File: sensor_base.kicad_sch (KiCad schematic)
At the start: 41 parts, among them J2 Conn_Coaxial, U1 MCP3204, U10 REF3040, U11 INA333xxDGK, U15 M24C02-WMN, U2 INA333xxDGK, U3 TPS22929D, U4 INA333xxDGK, U5 INA333xxDGK, U9 REF3025

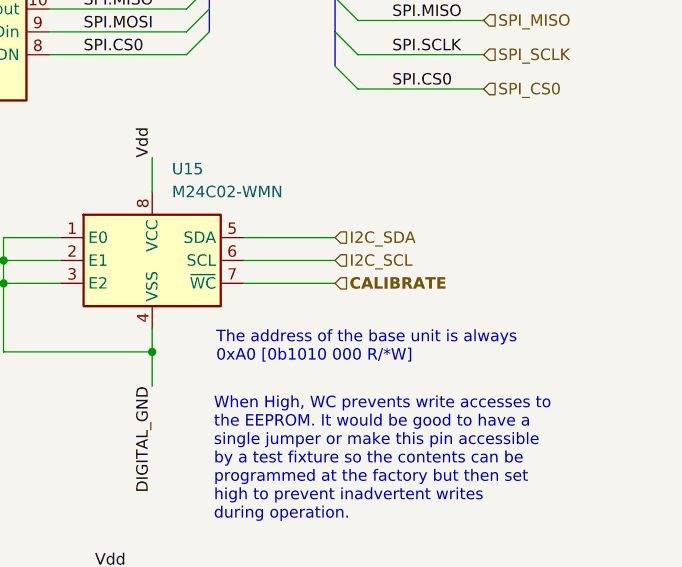
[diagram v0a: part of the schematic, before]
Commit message: Sensor board basic updates
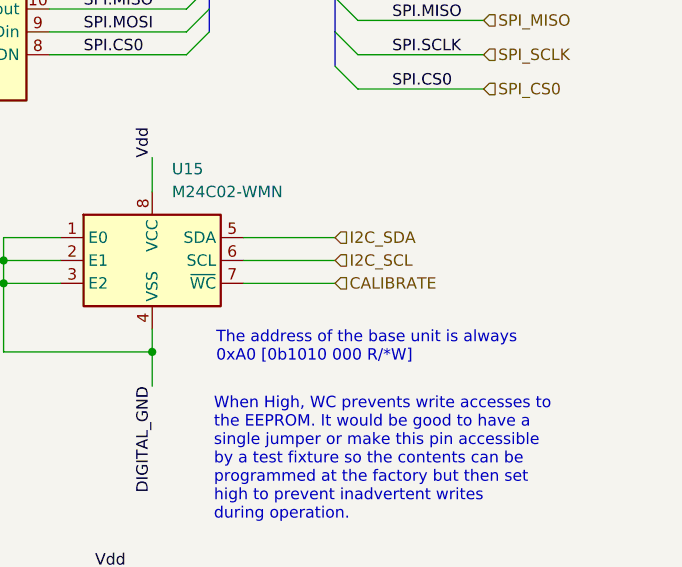
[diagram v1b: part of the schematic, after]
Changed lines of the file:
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@@
 			(font
 				(size 1.27 1.27)
-				(thickness 0.254)
-				(bold yes)
+				(thickness 0.1588)
 			)
 			(justify left)

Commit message: Split the sensor modules into a 4 and 8 port version. Fleshed out the power module a bit more. Started adding sensor board connectors to the root schematic and started pulling out sensor boards to their own, separate module. Began wiring up the root schematic to get my bearings a bit.
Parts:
- added C27, C28: C, symbol Device:C
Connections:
- net ANALOG_GND: now also C10.2, C11.2, C12.2, C13.2, C19.2, C21.2, C22.2, C5.2, C6.2, C7.2, C8.2, C9.2, C27.2, C28.2
- net DIGITAL_GND: now also C14.2, C15.2, C16.2, C17.2, C18.2, C20.2
- net Vdd: now also C10.1, C11.1, C12.1, C13.1, C14.1, C15.1, C16.1, C17.1, C18.1, C19.1, C20.1, C9.1
- net Vref_2.5: now also C21.1, C22.1, C5.1, C6.1
- net Vref_4.096: now also C7.1, C8.1, C27.1, C28.1
- net ENABLE/*SHDN renamed ENABLE/~{SHDN}
- net SPI_CS0 renamed SPI_CS
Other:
- note added: "Decoupling Capacitors are connected as close as possible to each IC of the given power domain."
- note added: "TBD"
- moved on the sheet: C14, C15, C16, C17, C18, C20, C21, C22, C5, C6, C7, C8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

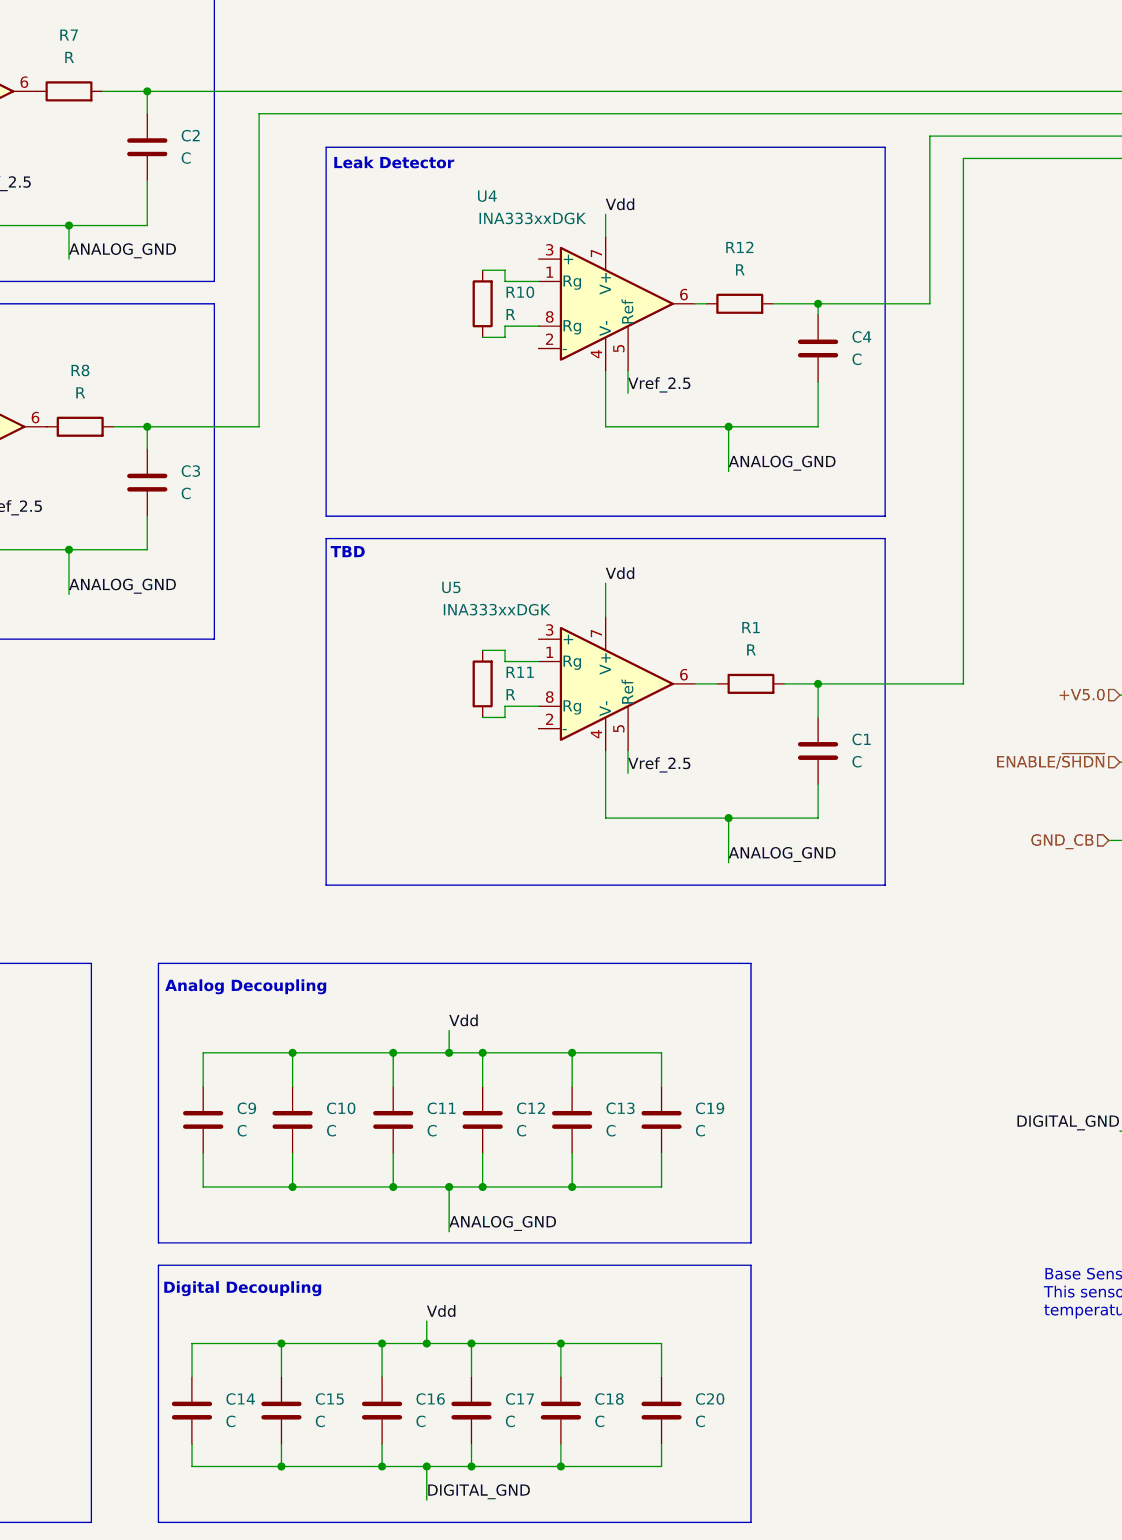
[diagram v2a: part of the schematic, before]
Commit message: Cleaned up some signal lines in the sensor board. Shuffled the decoupling caps around a bit as well as rearranged the EEPROM and power supply for clarity. Added buffered 2.5V offset to the pH and ORP circuits. Swapped one TBD input on the base sensor and sensor_4 boards for an ADC calibration input.
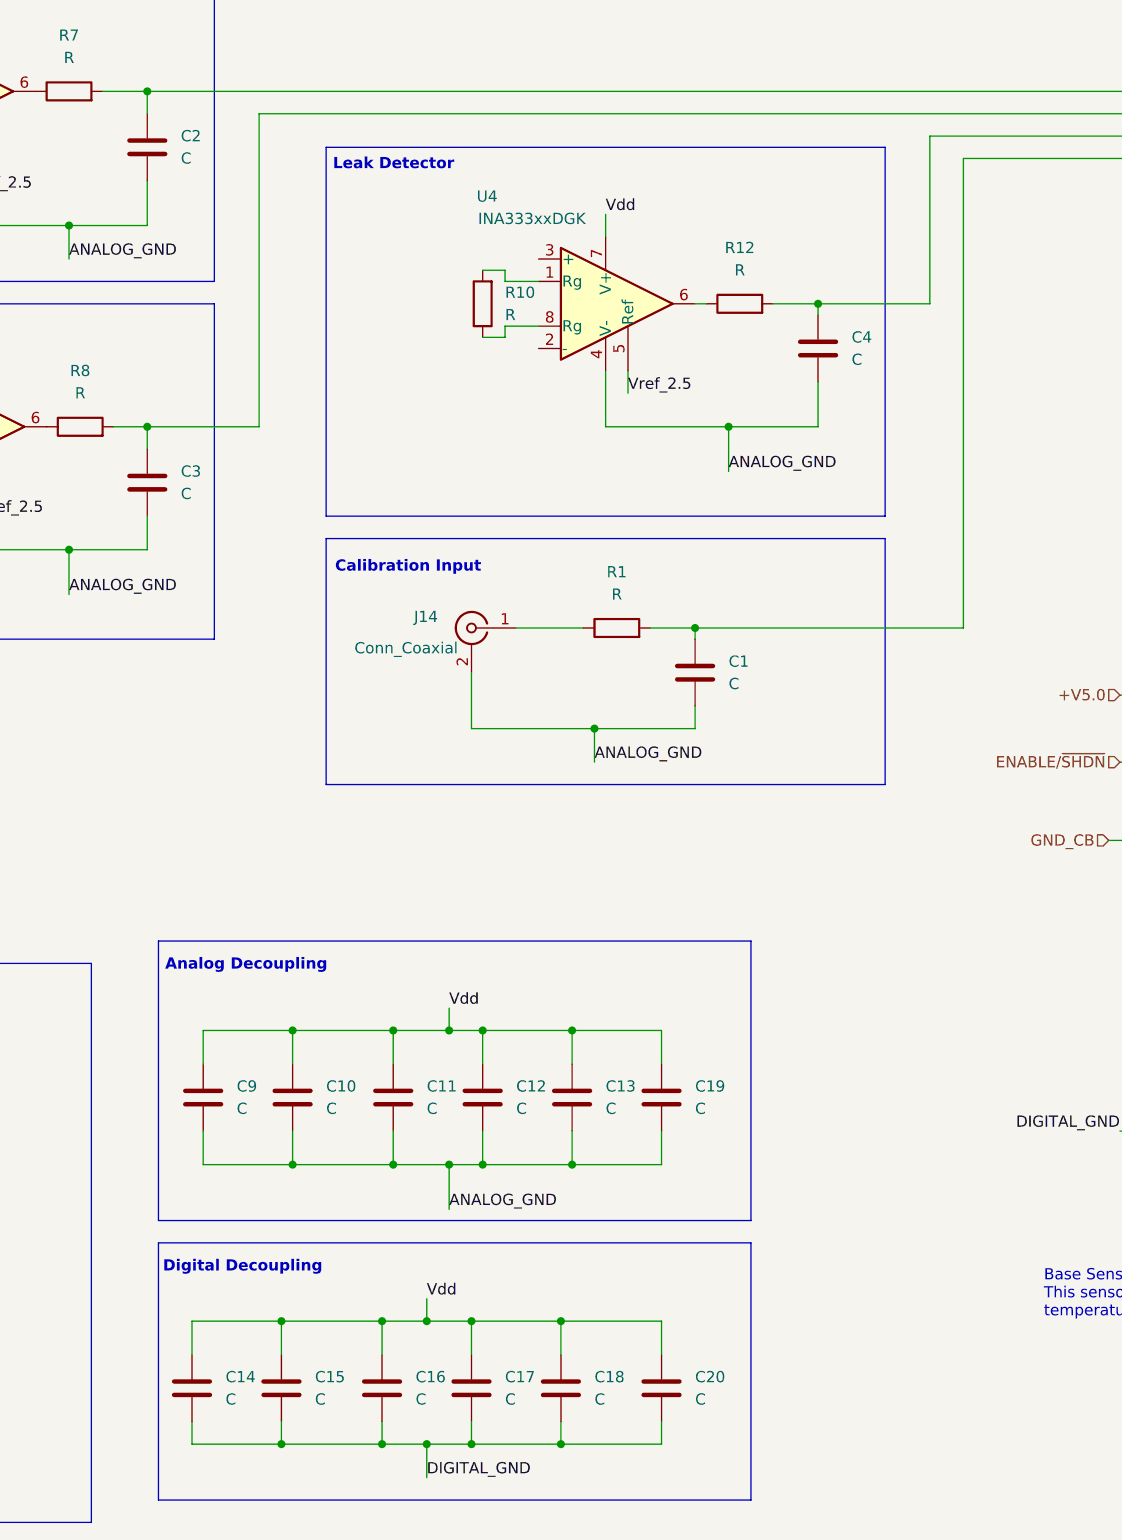
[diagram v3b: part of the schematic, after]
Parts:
- removed R11: R, symbol Device:R
- removed U5: INA333xxDGK, Package_SO:VSSOP-8_3x3mm_P0.65mm, symbol Amplifier_Instrumentation:INA333xxDGK
- added J14: Conn_Coaxial, symbol Connector:Conn_Coaxial
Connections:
- net ANALOG_GND: now also J14.2 (Ext)
- net at R1.1: now also J14.1 (In)
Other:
- note added: "Calibration Input"
- note removed: "TBD"
- moved on the sheet: C10, C11, C12, C13, C14, C15, C16, C17, C18, C19, C20, C9

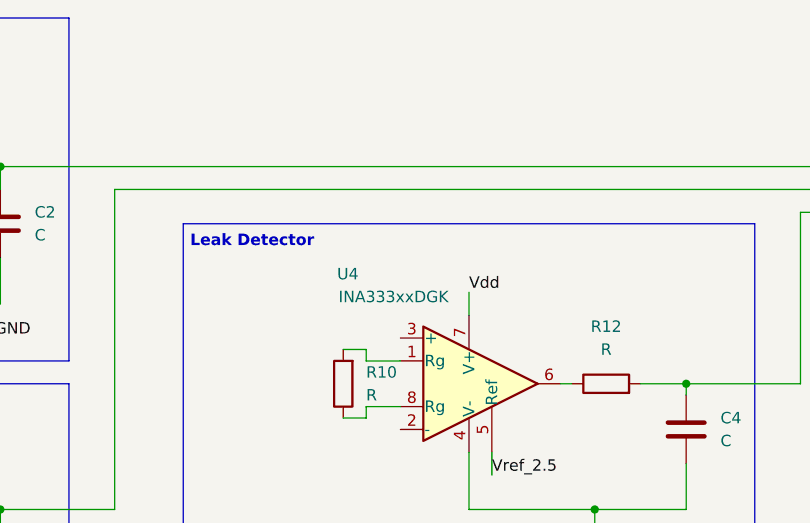
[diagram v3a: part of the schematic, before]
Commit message: Added some notes to otherwise blank pages. Added the full 8 sensor buffers to the 8 sensor analog board. Added a decoupling sub page to same. Changed a couple of sensor labels on base and 4 board just as placeholders
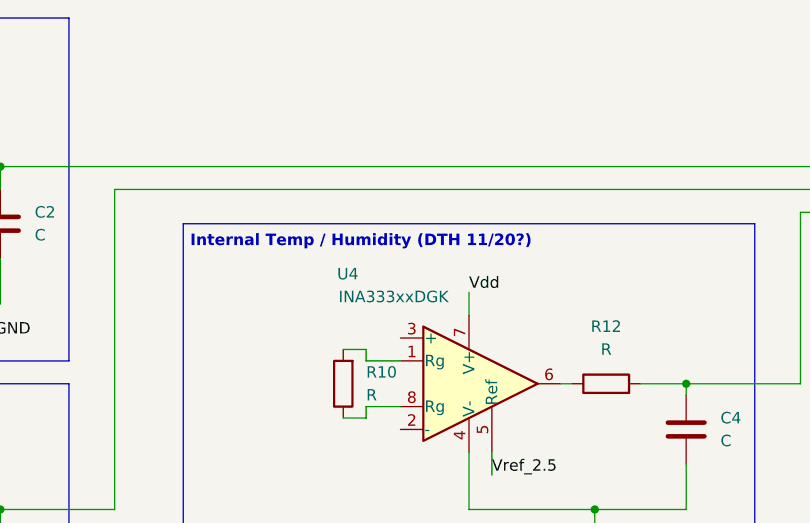
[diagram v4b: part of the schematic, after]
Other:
- note added: "Internal Temp / Humidity (DTH 11/20?)"
- note removed: "Leak Detector"
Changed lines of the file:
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@@
 		)
 	)
-	(text "Leak Detector"
+	(text "Internal Temp / Humidity (DTH 11/20?)"
 		(exclude_from_sim no)
 		(at 97.282 42.672 0)

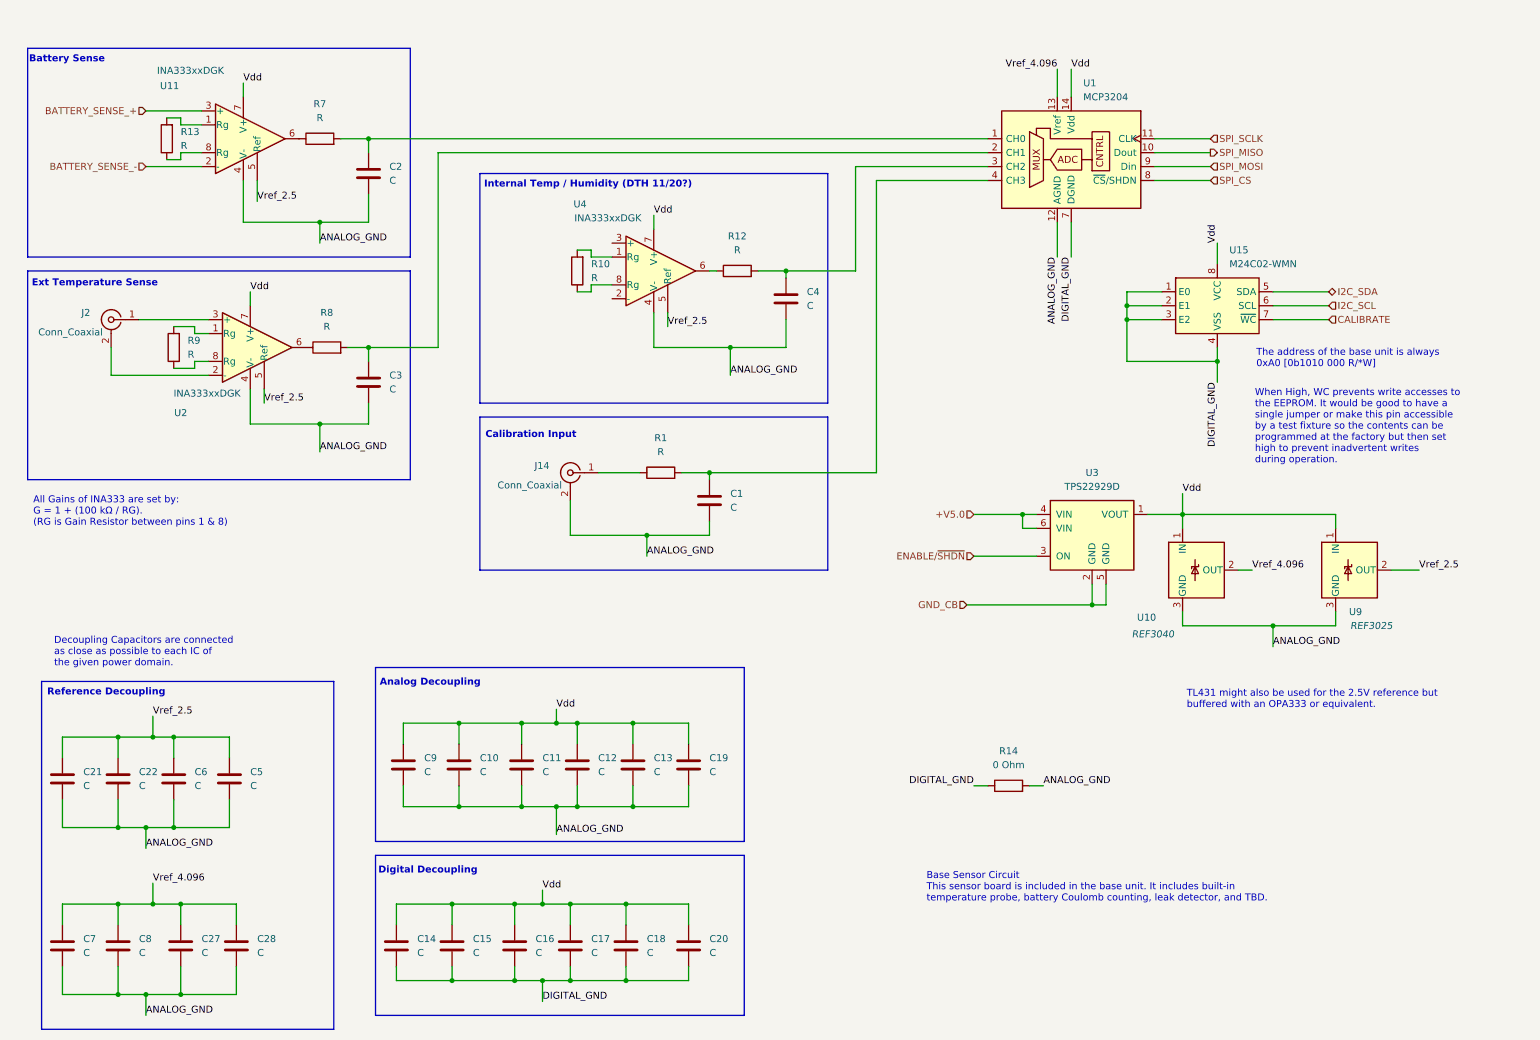
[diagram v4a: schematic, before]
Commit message: Updated the ORP and pH probes with a more appropriate amp. Added some notes. Added a tentative PL-100 adapter circuit. Added Vref buffering. Started move towards ESP32 ADC converter for base sensors.
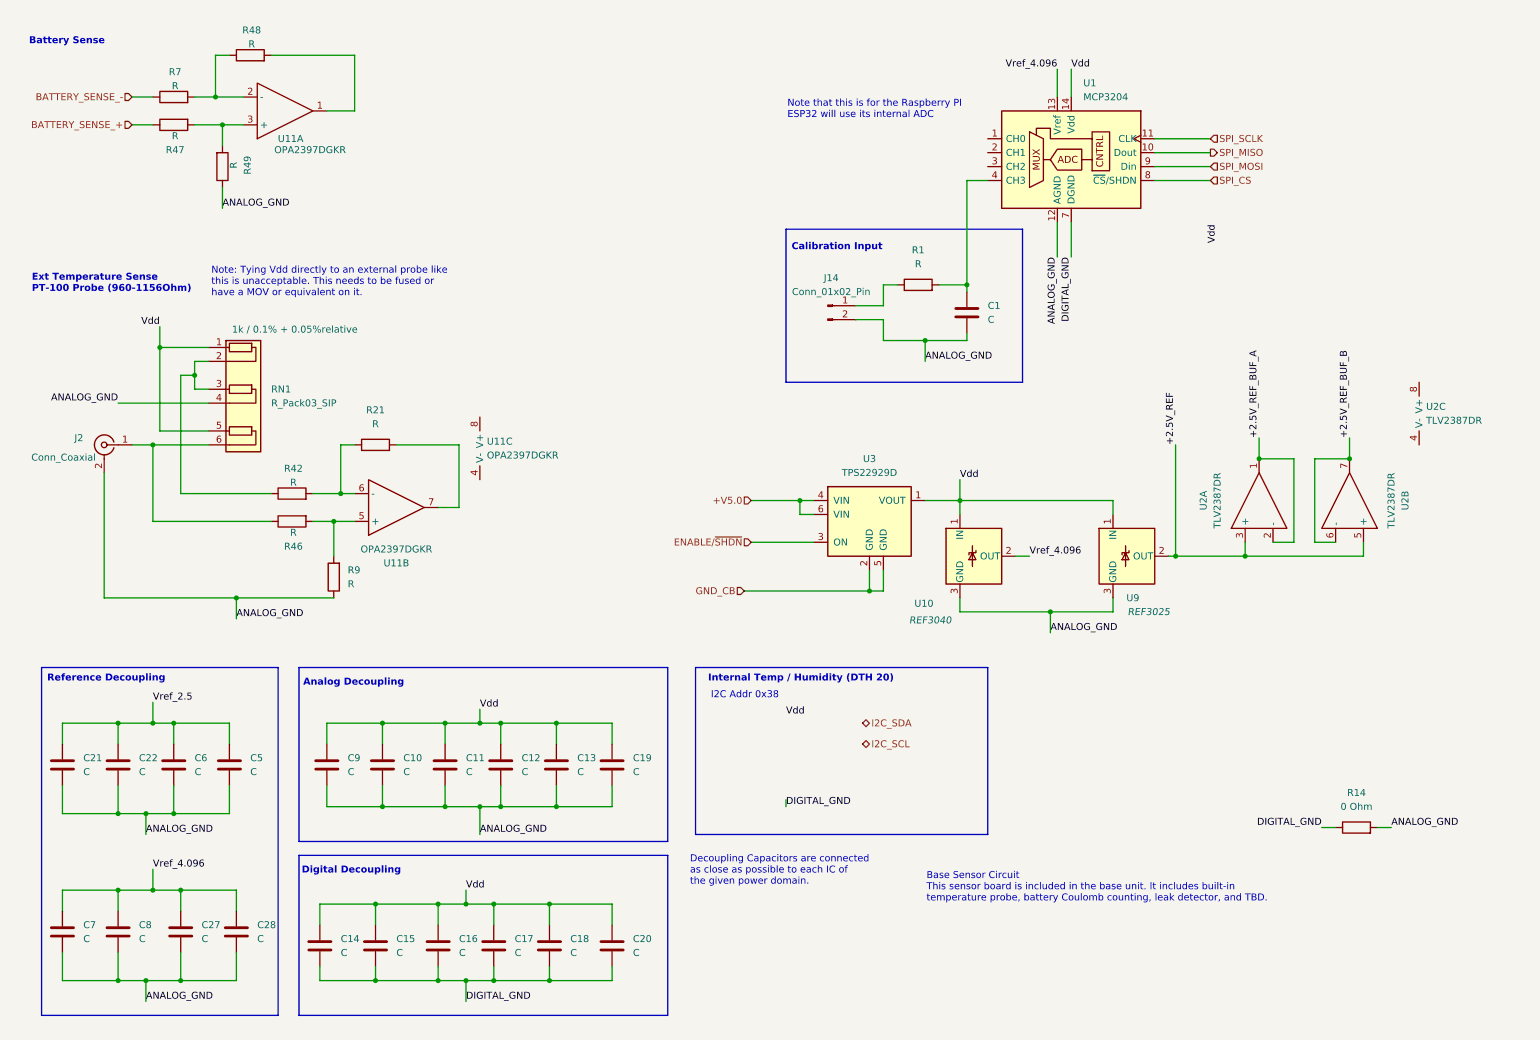
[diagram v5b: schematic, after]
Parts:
- removed C2, C3, C4: C, symbol Device:C
- removed J14: Conn_Coaxial, symbol Connector:Conn_Coaxial
- removed R10, R12, R13, R8: R, symbol Device:R
- removed U11, U2, U4: INA333xxDGK, Package_SO:VSSOP-8_3x3mm_P0.65mm, symbol Amplifier_Instrumentation:INA333xxDGK
- removed U15: M24C02-WMN, Package_SO:SOIC-8_3.9x4.9mm_P1.27mm, symbol Memory_EEPROM:M24C02-WMN
- added J14: Conn_01x02_Pin, symbol Connector:Conn_01x02_Pin
- added R21, R42, R46, R47, R48, R49: R, symbol Device:R
- added RN1: R_Pack03_SIP, Resistor_THT:R_Array_SIP6, symbol Device:R_Pack03_SIP
- added U11: OPA2397DGKR, Package_SO:SOIC-8_3.9x4.9mm_P1.27mm, symbol Op-Amp-Extended:OPA2397DR
- added U2: TLV2387DR, Package_SO:SOIC-8_3.9x4.9mm_P1.27mm, symbol Op-Amp-Extended:TLV2387DR
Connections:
- net ANALOG_GND: now also J2.2 (Ext), R9.1, J14.2 (Pin_2), R49.1, RN1.4 (R2.2)
- net BATTERY_SENSE_+: now also R47.1
- net BATTERY_SENSE_-: now also R7.1
- net Vdd: now also RN1.1 (R1.1), RN1.5 (R3.1)
- net Vref_2.5: no longer U9.2 (OUT)
- net at R7.2: now also R48.1, U11.2 (-); no longer U1.1 (CH0)
- net at J2.1 (In): now also R46.1, RN1.6 (R3.2)
- net at R1.1: now also J14.1 (Pin_1)
- net at R9.2: now also R46.2, U11.5 (+)
- new net: R48.2, U11.1
- new net: R21.1, R42.2, U11.6 (-)
- new net: R21.2, U11.7
- new net: R47.2, R49.2, U11.3 (+)
- new net: R42.1, RN1.2 (R1.2), RN1.3 (R2.1)
- new net +2.5V_REF: U2.3 (+), U2.5 (+), U9.2 (OUT)
- new net +2.5V_REF_BUF_A: U2.1, U2.2 (-)
- new net +2.5V_REF_BUF_B: U2.6 (-), U2.7
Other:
- note added: "Ext Temperature Sense PT-100 Probe (960-1156Ohm)"
- note added: "I2C Addr 0x38"
- note added: "Internal Temp / Humidity (DTH 20)"
- note added: "Note that this is for the Raspberry PI ESP32 will use its internal ADC"
- note added: "Note: Tying Vdd directly to an external probe like this is unacceptable. This needs to be fused or have a MOV or equivalent on it."
- note removed: "All Gains of INA333 are set by: G = 1 + (100 kΩ / RG). (RG is Gain Resistor between pins 1 & 8)"
- note removed: "Ext Temperature Sense"
- note removed: "Internal Temp / Humidity (DTH 11/20?)"
- note removed: "TL431 might also be used for the 2.5V reference but buffered with an OPA333 or equivalent."
- note removed: "The address of the base unit is always 0xA0 [0b1010 000 R/*W]"
- note removed: "When High, WC prevents write accesses to the EEPROM. It would be good to have a single jumper or make this pin accessible by a test fixture so the contents can be programmed at the factory but then set high to prevent inadvertent writes during operation."
- moved on the sheet: C1, C10, C11, C12, C13, C14, C15, C16, C17, C18, C19, C20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
